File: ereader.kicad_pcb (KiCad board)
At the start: 4 copper layers, 66 x 115 mm, 81 parts, among them J1 USB-C-16P, J2 EPD_FPC_24P, J3 FL_FPC_6P, J4 microSD, J5 Battery_1S, SW1 BTN_A, SW2 BTN_B, SW3 BTN_C, SW4 SLLB510200, U1 ESP32-S3-WROOM-1-N16R8, U2 BQ25628E, U3 MAX17048, U4 LM3630A, U5 TPS62840, U6 USBLC6-2SC6

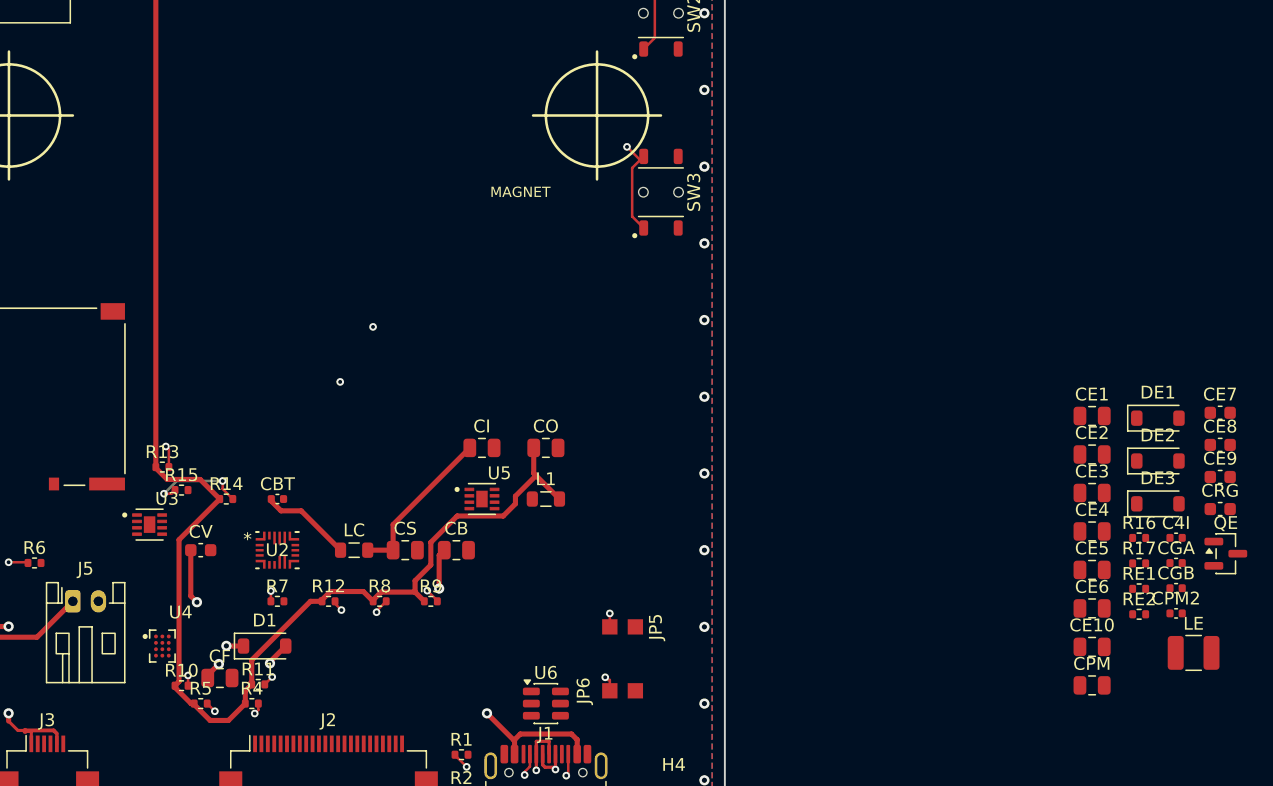
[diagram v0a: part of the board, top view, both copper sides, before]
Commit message: place the 25 imported parts (charger/buck/gauge decoupling + EPD DC-DC)
The netlist import left the new parts stacked off-board at X~94-105. Placed
all 25 onto the board, grouped by subsystem, verified collision-free (no
courtyard overlap among any of the 81 footprints; kept clear of the antenna
and microSD keep-outs and >=0.5mm off the board edge):

- Decoupling next to its IC: CGA/CGB by U3 (CELL), CRG/CPM/CPM2 by U2
  (REGN/PMID), R17 (ILIM) by U2, R16 (VSET) by U5, C4I by U4.
- EPD DC-DC as one compact block (LE, QE, DE1-3, RE1/2, CE1-10) in the open
  mid-board region (X~20-48, Y~56-67) -- the only contiguous free area; it
  sits on clean copper (0 existing traces there) so it routes fresh.

Notes for routing (mine to flag, yours to finish):
- The EPD block is ~40mm above J2; the +/-20V rails will be long -- tighten
  toward J2 if you can free space, and keep those loops short.
- The charger/buck decoupling landed in the already-routed power area whose
  old traces are invalid after the footprint swaps -- rip up and re-route.
- I can't render/DRC here, so this is a collision-free starting placement;
  eyeball orientations and run DRC before/after routing.

Co-Authored-By: Claude Opus 4.8 <noreply@anthropic.com>
Claude-Session: https://claude.ai/code/session_01YVjCqztAZrXZoCUDKGWwAc
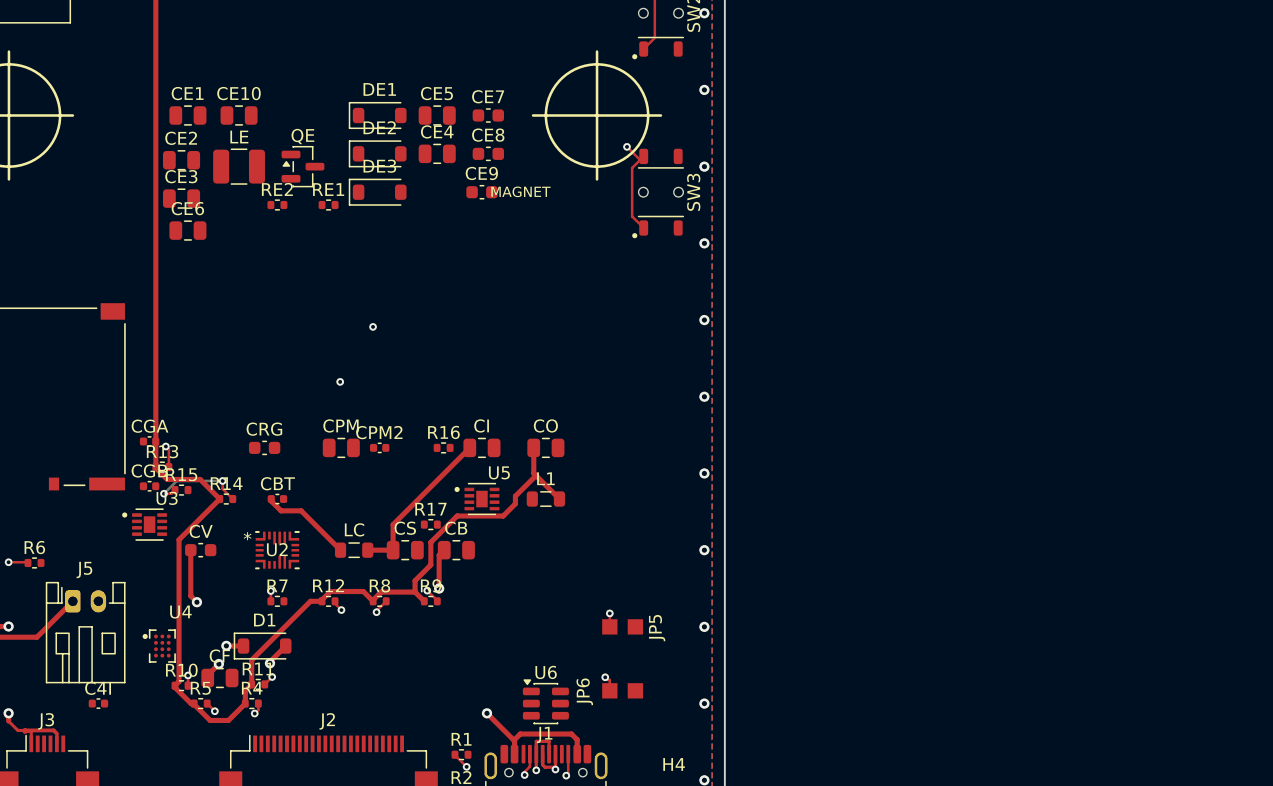
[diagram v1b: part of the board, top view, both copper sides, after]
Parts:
- moved C4I 85.3 mm to (17.0, 104.0)
- moved LE 83.8 mm to (28.0, 62.0)
- moved CGA 80.9 mm to (21.0, 83.5)
- moved CGB 80.7 mm to (21.0, 87.0)
- moved CE10 78.6 mm to (28.0, 58.0)
- moved QE 78.3 mm to (33.0, 62.0)
- moved CE6 76.7 mm to (24.0, 67.0)
- moved CRG 74.9 mm to (30.0, 84.0)
- moved CE3 74.9 mm to (23.5, 64.5)
- moved CE2 74.9 mm to (23.5, 61.5)
- moved RE2 74.6 mm to (31.0, 65.0)
- moved CE1 74.5 mm to (24.0, 58.0)
- moved RE1 70.2 mm to (35.0, 65.0)
- moved DE3 65.6 mm to (39.0, 64.0)
- moved DE2 65.4 mm to (39.0, 61.0)
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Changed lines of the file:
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@@
 	(footprint "Capacitor_SMD:C_0603_1608Metric"
 		(layer "F.Cu")
-		(at 104.745 86.275)
+		(at 47 64)
 		(descr "Capacitor SMD 0603 (1608 Metric), square (rectangular) end terminal, IPC-7351 nominal, (Body size source: IPC-SM-782 page 76, https://www.pcb-3d.com/wordpress/wp-content/uploads/ipc-sm-782a_amendment_1_and_2.pdf)")
 		(tags "capacitor")
@@
 	(footprint "Capacitor_SMD:C_0805_2012Metric"
 		(layer "F.Cu")
-		(at 94.725 81.505)
+		(at 24 58)
 		(descr "Capacitor SMD 0805 (2012 Metric), square (rectangular) end terminal, IPC-7351 nominal, (Body size source: IPC-SM-782 page 76, https://www.pcb-3d.com/wordpress/wp-content/uploads/ipc-sm-782a_amendment_1_and_2.pdf, https://docs.google.com/spreadsheets/d/1BsfQQcO9C6DZCsRaXUlFlo91Tg2WpOkGARC1WS5S8t0/edit?usp=sharing)")
 		(tags "capacitor")
@@
 	(footprint "Capacitor_SMD:C_0805_2012Metric"
 		(layer "F.Cu")
-		(at 94.725 84.515)
+		(at 23.5 61.5)
 		(descr "Capacitor SMD 0805 (2012 Metric), square (rectangular) end terminal, IPC-7351 nominal, (Body size source: IPC-SM-782 page 76, https://www.pcb-3d.com/wordpress/wp-content/uploads/ipc-sm-782a_amendment_1_and_2.pdf, https://docs.google.com/spreadsheets/d/1BsfQQcO9C6DZCsRaXUlFlo91Tg2WpOkGARC1WS5S8t0/edit?usp=sharing)")
 		(tags "capacitor")
@@
 	(footprint "Capacitor_SMD:C_0805_2012Metric"
 		(layer "F.Cu")
-		(at 94.725 93.545)
+		(at 43.5 58)
 		(descr "Capacitor SMD 0805 (2012 Metric), square (rectangular) end terminal, IPC-7351 nominal, (Body size source: IPC-SM-782 page 76, https://www.pcb-3d.com/wordpress/wp-content/uploads/ipc-sm-782a_amendment_1_and_2.pdf, https://docs.google.com/spreadsheets/d/1BsfQQcO9C6DZCsRaXUlFlo91Tg2WpOkGARC1WS5S8t0/edit?usp=sharing)")
 		(tags "capacitor")
@@
 	(footprint "Capacitor_SMD:C_0402_1005Metric"
 		(layer "F.Cu")
-		(at 101.295 93.005)
+		(at 21 83.5)
 		(descr "Capacitor SMD 0402 (1005 Metric), square (rectangular) end terminal, IPC-7351 nominal, (Body size source: IPC-SM-782 page 76, https://www.pcb-3d.com/wordpress/wp-content/uploads/ipc-sm-782a_amendment_1_and_2.pdf)")
 		(tags "capacitor")
@@
 	(footprint "Capacitor_SMD:C_0402_1005Metric"
 		(layer "F.Cu")
-		(at 101.295 96.945)
+		(at 39 84)
 		(descr "Capacitor SMD 0402 (1005 Metric), square (rectangular) end terminal, IPC-7351 nominal, (Body size source: IPC-SM-782 page 76, https://www.pcb-3d.com/wordpress/wp-content/uploads/ipc-sm-782a_amendment_1_and_2.pdf)")
 		(tags "capacitor")
@@
 	(footprint "Capacitor_SMD:C_0805_2012Metric"
 		(layer "F.Cu")
-		(at 94.725 96.555)
+		(at 24 67)
 		(descr "Capacitor SMD 0805 (2012 Metric), square (rectangular) end terminal, IPC-7351 nominal, (Body size source: IPC-SM-782 page 76, https://www.pcb-3d.com/wordpress/wp-content/uploads/ipc-sm-782a_amendment_1_and_2.pdf, https://docs.google.com/spreadsheets/d/1BsfQQcO9C6DZCsRaXUlFlo91Tg2WpOkGARC1WS5S8t0/edit?usp=sharing)")
 		(tags "capacitor")
@@
 	(footprint "Resistor_SMD:R_0402_1005Metric"
 		(layer "F.Cu")
-		(at 98.405 95.025)
+		(at 35 65)
 		(descr "Resistor SMD 0402 (1005 Metric), square (rectangular) end terminal, IPC-7351 nominal, (Body size source: IPC-SM-782 page 72, https://www.pcb-3d.com/wordpress/wp-content/uploads/ipc-sm-782a_amendment_1_and_2.pdf)")
 		(tags "resistor")
@@
 	(footprint "Inductor_SMD:L_1210_3225Metric"
 		(layer "F.Cu")
-		(at 102.665 100.035)
+		(at 28 62)
 		(descr "Inductor SMD 1210 (3225 Metric), square (rectangular) end terminal, IPC-7351 nominal, (Body size source: http://www.tortai-tech.com/upload/download/2011102023233369053.pdf)")
 		(tags "inductor")
@@
 	(footprint "Diode_SMD:D_SOD-123"
 		(layer "F.Cu")
-		(at 99.87 88.375)
+		(at 39 64)
 		(descr "SOD-123")
 		(tags "SOD-123")
@@
 	(footprint "Resistor_SMD:R_0402_1005Metric"
 		(layer "F.Cu")
-		(at 98.405 97.015)
+		(at 31 65)
 		(descr "Resistor SMD 0402 (1005 Metric), square (rectangular) end terminal, IPC-7351 nominal, (Body size source: IPC-SM-782 page 72, https://www.pcb-3d.com/wordpress/wp-content/uploads/ipc-sm-782a_amendment_1_and_2.pdf)")
 		(tags "resistor")
@@
 	(footprint "Capacitor_SMD:C_0805_2012Metric"
 		(layer "F.Cu")
-		(at 94.725 90.535)
+		(at 43.5 61)
 		(descr "Capacitor SMD 0805 (2012 Metric), square (rectangular) end terminal, IPC-7351 nominal, (Body size source: IPC-SM-782 page 76, https://www.pcb-3d.com/wordpress/wp-content/uploads/ipc-sm-782a_amendment_1_and_2.pdf, https://docs.google.com/spreadsheets/d/1BsfQQcO9C6DZCsRaXUlFlo91Tg2WpOkGARC1WS5S8t0/edit?usp=sharing)")
 		(tags "capacitor")
@@
 	(footprint "Diode_SMD:D_SOD-123"
 		(layer "F.Cu")
-		(at 99.87 81.675)
+		(at 39 58)
 		(descr "SOD-123")
 		(tags "SOD-123")
@@
 	(footprint "Capacitor_SMD:C_0402_1005Metric"
 		(layer "F.Cu")
-		(at 101.295 91.035)
+		(at 17 104)
 		(descr "Capacitor SMD 0402 (1005 Metric), square (rectangular) end terminal, IPC-7351 nominal, (Body size source: IPC-SM-782 page 76, https://www.pcb-3d.com/wordpress/wp-content/uploads/ipc-sm-782a_amendment_1_and_2.pdf)")
 		(tags "capacitor")
@@
 	(footprint "Capacitor_SMD:C_0402_1005Metric"
 		(layer "F.Cu")
-		(at 101.295 94.975)
+		(at 21 87)
 		(descr "Capacitor SMD 0402 (1005 Metric), square (rectangular) end terminal, IPC-7351 nominal, (Body size source: IPC-SM-782 page 76, https://www.pcb-3d.com/wordpress/wp-content/uploads/ipc-sm-782a_amendment_1_and_2.pdf)")
 		(tags "capacitor")
@@
 	(footprint "Capacitor_SMD:C_0805_2012Metric"
 		(layer "F.Cu")
-		(at 94.725 87.525)
+		(at 23.5 64.5)
 		(descr "Capacitor SMD 0805 (2012 Metric), square (rectangular) end terminal, IPC-7351 nominal, (Body size source: IPC-SM-782 page 76, https://www.pcb-3d.com/wordpress/wp-content/uploads/ipc-sm-782a_amendment_1_and_2.pdf, https://docs.google.com/spreadsheets/d/1BsfQQcO9C6DZCsRaXUlFlo91Tg2WpOkGARC1WS5S8t0/edit?usp=sharing)")
 		(tags "capacitor")
@@
 	(footprint "Capacitor_SMD:C_0805_2012Metric"
 		(layer "F.Cu")
-		(at 94.725 102.575)
+		(at 36 84)
 		(descr "Capacitor SMD 0805 (2012 Metric), square (rectangular) end terminal, IPC-7351 nominal, (Body size source: IPC-SM-782 page 76, https://www.pcb-3d.com/wordpress/wp-content/uploads/ipc-sm-782a_amendment_1_and_2.pdf, https://docs.google.com/spreadsheets/d/1BsfQQcO9C6DZCsRaXUlFlo91Tg2WpOkGARC1WS5S8t0/edit?usp=sharing)")
 		(tags "capacitor")
@@
 	(footprint "Package_TO_SOT_SMD:SOT-23"
 		(layer "F.Cu")
-		(at 105.185 92.275)
+		(at 33 62)
 		(descr "SOT, 3 Pin (JEDEC TO-236 Var AB https://www.jedec.org/document_search?search_api_views_fulltext=TO-236)")
 		(tags "SOT TO_SOT_SMD")
@@
 	(footprint "Diode_SMD:D_SOD-123"
 		(layer "F.Cu")
-		(at 99.87 85.025)
+		(at 39 61)
 		(descr "SOD-123")
 		(tags "SOD-123")
@@
 	(footprint "Capacitor_SMD:C_0603_1608Metric"
 		(layer "F.Cu")
-		(at 104.745 88.785)
+		(at 30 84)
 		(descr "Capacitor SMD 0603 (1608 Metric), square (rectangular) end terminal, IPC-7351 nominal, (Body size source: IPC-SM-782 page 76, https://www.pcb-3d.com/wordpress/wp-content/uploads/ipc-sm-782a_amendment_1_and_2.pdf)")
 		(tags "capacitor")
@@
 	(footprint "Resistor_SMD:R_0402_1005Metric"
 		(layer "F.Cu")
-		(at 98.405 91.045)
+		(at 44 84)
 		(descr "Resistor SMD 0402 (1005 Metric), square (rectangular) end terminal, IPC-7351 nominal, (Body size source: IPC-SM-782 page 72, https://www.pcb-3d.com/wordpress/wp-content/uploads/ipc-sm-782a_amendment_1_and_2.pdf)")
 		(tags "resistor")
@@
 	(footprint "Capacitor_SMD:C_0603_1608Metric"
 		(layer "F.Cu")
-		(at 104.745 83.765)
+		(at 47.5 61)
 		(descr "Capacitor SMD 0603 (1608 Metric), square (rectangular) end terminal, IPC-7351 nominal, (Body size source: IPC-SM-782 page 76, https://www.pcb-3d.com/wordpress/wp-content/uploads/ipc-sm-782a_amendment_1_and_2.pdf)")
 		(tags "capacitor")
@@
 	(footprint "Capacitor_SMD:C_0805_2012Metric"
 		(layer "F.Cu")
-		(at 94.725 99.565)
+		(at 28 58)
 		(descr "Capacitor SMD 0805 (2012 Metric), square (rectangular) end terminal, IPC-7351 nominal, (Body size source: IPC-SM-782 page 76, https://www.pcb-3d.com/wordpress/wp-content/uploads/ipc-sm-782a_amendment_1_and_2.pdf, https://docs.google.com/spreadsheets/d/1BsfQQcO9C6DZCsRaXUlFlo91Tg2WpOkGARC1WS5S8t0/edit?usp=sharing)")
 		(tags "capacitor")
@@
 	(footprint "Capacitor_SMD:C_0603_1608Metric"
 		(layer "F.Cu")
-		(at 104.745 81.255)
+		(at 47.5 58)
 		(descr "Capacitor SMD 0603 (1608 Metric), square (rectangular) end terminal, IPC-7351 nominal, (Body size source: IPC-SM-782 page 76, https://www.pcb-3d.com/wordpress/wp-content/uploads/ipc-sm-782a_amendment_1_and_2.pdf)")
 		(tags "capacitor")
@@
 	(footprint "Resistor_SMD:R_0402_1005Metric"
 		(layer "F.Cu")
-		(at 98.405 93.035)
+		(at 43 90)
 		(descr "Resistor SMD 0402 (1005 Metric), square (rectangular) end terminal, IPC-7351 nominal, (Body size source: IPC-SM-782 page 72, https://www.pcb-3d.com/wordpress/wp-content/uploads/ipc-sm-782a_amendment_1_and_2.pdf)")
 		(tags "resistor")
